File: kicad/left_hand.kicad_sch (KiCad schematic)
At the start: 31 parts, among them SW10 Gateron_ks_27, SW11 Gateron_ks_27, SW12 Gateron_ks_27, SW13 Gateron_ks_27, SW14 Gateron_ks_27, SW15 Gateron_ks_27, SW16 Gateron_ks_27, SW17 Gateron_ks_27, SW18 Gateron_ks_27, SW19 Gateron_ks_27, SW20 Gateron_ks_27, SW21 Gateron_ks_27, SW22 Gateron_ks_27, SW23 Gateron_ks_27, SW24 Gateron_ks_27, SW25 Gateron_ks_27, SW26 Gateron_ks_27, SW27 Gateron_ks_27, SW28 Gateron_ks_27, SW29 Gateron_ks_27, SW30 Gateron_ks_27, SW31 Gateron_ks_27, SW32 Gateron_ks_27, SW33 Gateron_ks_27, SW4 Gateron_ks_27, SW5 Gateron_ks_27, SW6 Gateron_ks_27, SW7 Gateron_ks_27, SW8 Gateron_ks_27, SW9 Gateron_ks_27, U2 74HC595

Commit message: Update PCB
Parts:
- added D1, D10, D11, D12, D13, D14, D15, D16, D17, D18, D19, D2, D20, D21, D22, D23, D24, D25, D26, D27, D28, D29, D3, D30, D4, D5, D6, D7, D8, D9: 1N4148W, Diode_SMD:D_SOD-123, symbol Diode:1N4148W-JLC
- SW10, SW11, SW12, SW13, SW14, SW15, SW16, SW17, SW18, SW19, SW20, SW21, SW22, SW23, SW24, SW25, SW26, SW27, SW28, SW29, SW30, SW31, SW32, SW33, SW4, SW5, SW6, SW7, SW8, SW9: now not fitted
- U2: LCSC (none) -> C72115
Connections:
- net ROW1: now also D1.1 (K), D2.1 (K), D3.1 (K), D4.1 (K), D5.1 (K), D6.1 (K), D7.1 (K); no longer SW10.3 (K), SW14.3 (K), SW18.3 (K), SW22.3 (K), SW26.3 (K), SW30.3 (K), SW6.3 (K)
- net ROW2: now also D10.1 (K), D11.1 (K), D12.1 (K), D13.1 (K), D14.1 (K), D8.1 (K), D9.1 (K); no longer SW11.3 (K), SW15.3 (K), SW19.3 (K), SW23.3 (K), SW27.3 (K), SW31.3 (K), SW7.3 (K)
- net ROW3: now also D15.1 (K), D16.1 (K), D17.1 (K), D18.1 (K), D19.1 (K), D20.1 (K), D21.1 (K), D22.1 (K); no longer SW12.3 (K), SW16.3 (K), SW20.3 (K), SW24.3 (K), SW28.3 (K), SW32.3 (K), SW4.3 (K), SW8.3 (K)
- net ROW4: now also D23.1 (K), D24.1 (K), D25.1 (K), D26.1 (K), D27.1 (K), D28.1 (K), D29.1 (K), D30.1 (K); no longer SW13.3 (K), SW17.3 (K), SW21.3 (K), SW25.3 (K), SW29.3 (K), SW33.3 (K), SW5.3 (K), SW9.3 (K)
- net at SW27.1: now also D13.2 (A); no longer SW27.4 (A)
- net at SW15.1: now also D10.2 (A); no longer SW15.4 (A)
- net at SW19.1: now also D11.2 (A); no longer SW19.4 (A)
- net at SW13.1: now also D25.2 (A); no longer SW13.4 (A)
- net at SW22.1: now also D5.2 (A); no longer SW22.4 (A)
- net at SW5.1: now also D23.2 (A); no longer SW5.4 (A)
- net at SW30.1: now also D7.2 (A); no longer SW30.4 (A)
- net at SW24.1: now also D20.2 (A); no longer SW24.4 (A)
- net at SW33.1: now also D30.2 (A); no longer SW33.4 (A)
- net at SW28.1: now also D21.2 (A); no longer SW28.4 (A)
- net at SW4.1: now also D15.2 (A); no longer SW4.4 (A)
- net at SW23.1: now also D12.2 (A); no longer SW23.4 (A)
- net at SW26.1: now also D6.2 (A); no longer SW26.4 (A)
- net at SW17.1: now also D26.2 (A); no longer SW17.4 (A)
- net at SW18.1: now also D4.2 (A); no longer SW18.4 (A)
- net at SW7.1: now also D8.2 (A); no longer SW7.4 (A)
- net at SW11.1: now also D9.2 (A); no longer SW11.4 (A)
- net at SW29.1: now also D29.2 (A); no longer SW29.4 (A)
- net at SW31.1: now also D14.2 (A); no longer SW31.4 (A)
- net at SW6.1: now also D1.2 (A); no longer SW6.4 (A)
- net at SW25.1: now also D28.2 (A); no longer SW25.4 (A)
- net at SW20.1: now also D19.2 (A); no longer SW20.4 (A)
- net at SW9.1: now also D24.2 (A); no longer SW9.4 (A)
- net at SW16.1: now also D18.2 (A); no longer SW16.4 (A)
- net at SW8.1: now also D16.2 (A); no longer SW8.4 (A)
- net at SW10.1: now also D2.2 (A); no longer SW10.4 (A)
- net at SW21.1: now also D27.2 (A); no longer SW21.4 (A)
- net at SW12.1: now also D17.2 (A); no longer SW12.4 (A)
- net at SW14.1: now also D3.2 (A); no longer SW14.4 (A)
- net at SW32.1: now also D22.2 (A); no longer SW32.4 (A)

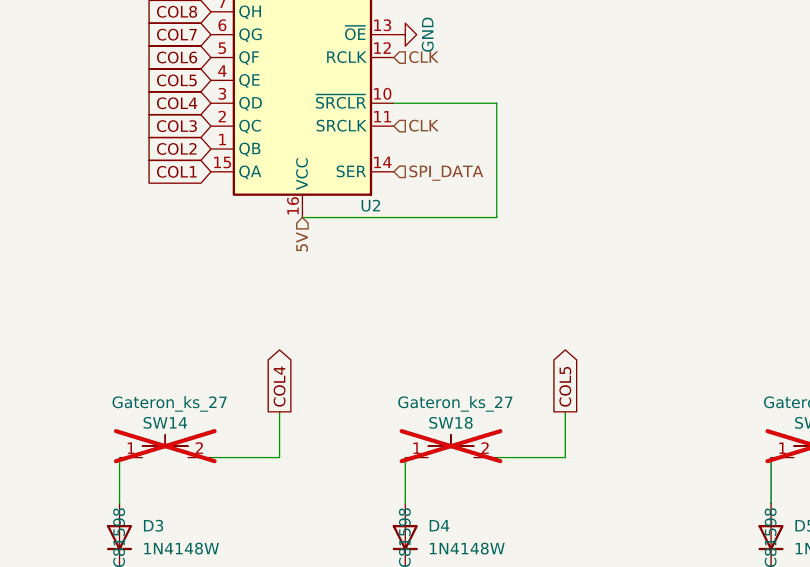
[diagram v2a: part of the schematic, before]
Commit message: SIPO is SMT
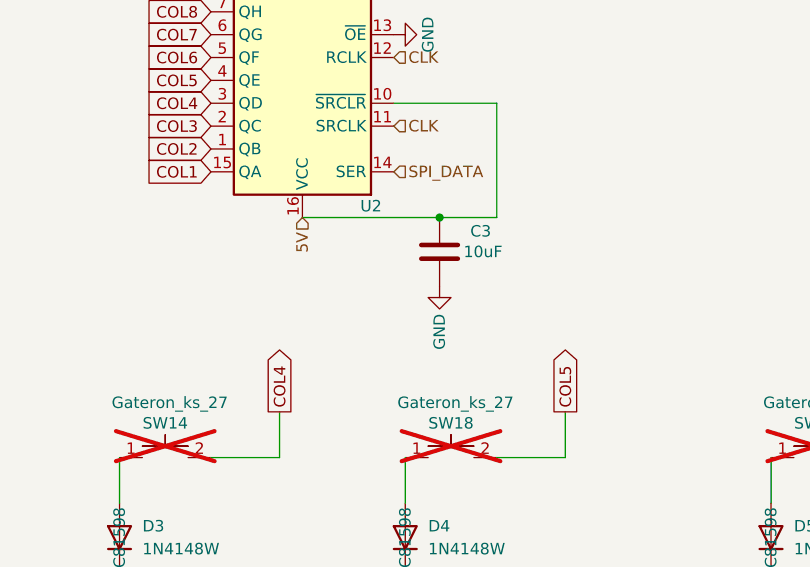
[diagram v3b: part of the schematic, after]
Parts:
- added C3: 10uF, Capacitor_SMD:C_0603_1608Metric, symbol Device:C
- U2: footprint Package_DIP:DIP-16_W7.62mm_Socket -> Package_SO:SO-16_3.9x9.9mm_P1.27mm; LCSC C72115 -> C5947
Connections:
- net 5V: now also C3.1
- net GND: now also C3.2
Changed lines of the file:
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@@
 	)
 	(junction
+		(at 208.28 90.17)
+		(diameter 0)
+		(color 0 0 0 0)
+	)
+	(junction
 		(at 107.95 227.33)
 		(diameter 0)
@@
 	(wire
 		(pts
-			(xy 214.63 90.17) (xy 193.04 90.17)
+			(xy 214.63 90.17) (xy 208.28 90.17)
 		)
 		(stroke
@@
 	(wire
 		(pts
+			(xy 208.28 90.17) (xy 193.04 90.17)
+		)
+		(stroke
+			(width 0)
+			(type default)
+		)
+	)
+	(wire
+		(pts
 			(xy 140.97 227.33) (xy 172.72 227.33)
 		)
@@
 	(symbol
 		(lib_id "power:GND")
+		(at 208.28 97.79 0)
+		(unit 1)
+		(exclude_from_sim no)
+		(in_bom yes)
+		(on_board yes)
+		(dnp no)
+		(property "Reference" "#PWR05"
+			(at 208.28 104.14 0)
+			(effects
+				(font
+					(size 1.27 1.27)
+				)
+				(hide yes)
+			)
+		)
+		(property "Value" "GND"
+			(at 208.28 102.87 90)
+			(effects
+				(font
+					(size 1.27 1.27)
+				)
+			)
+		)
+		(property "Footprint" ""
+			(at 208.28 97.79 0)
+			(effects
+				(font
+					(size 1.27 1.27)
+				)
+				(hide yes)
+			)
+		)
+		(property "Datasheet" ""
+			(at 208.28 97.79 0)
+			(effects
+				(font
+					(size 1.27 1.27)
+				)
+				(hide yes)
+			)
+		)
+		(property "Description" "Power symbol creates a global label with name \"GND\" , ground"
+			(at 208.28 97.79 0)
+			(effects
+				(font
+					(size 1.27 1.27)
+				)
+				(hide yes)
+			)
+		)
+		(pin "1"
+		)
+		(instances
+			(project "keyboard"
+				(path "/b0ce3c94-e169-4400-82ce-8ef44a8a59a3/f6761ea6-a0c4-4238-8bcb-bb4bd82c6051"
+					(reference "#PWR05")
+					(unit 1)
+				)
+			)
+		)
+	)
+	(symbol
+		(lib_id "power:GND")
 		(at 193.04 57.15 180)
 		(unit 1)
@@
 			)
 		)
-		(property "Footprint" "Package_DIP:DIP-16_W7.62mm_Socket"
+		(property "Footprint" "Package_SO:SO-16_3.9x9.9mm_P1.27mm"
 			(at 193.04 74.93 0)
 			(effects
@@
 			)
 		)
-		(property "LCSC" "C72115"
+		(property "LCSC" "C5947"
 			(at 193.04 74.93 0)
 			(effects
@@
 					(unit 1)
 				)
+			)
+		)
+	)
+	(symbol
+		(lib_id "Device:C")
+		(at 208.28 93.98 0)
+		(unit 1)
+		(exclude_from_sim no)
+		(in_bom yes)
+		(on_board yes)
+		(dnp no)
+		(property "Reference" "C3"
+			(at 212.852 91.694 0)
+			(effects
+				(font
+					(size 1.27 1.27)
+				)
+			)
+		)
+		(property "Value" "10uF"
+			(at 213.106 93.98 0)
+			(effects
+				(font
+					(size 1.27 1.27)
+				)
+			)
+		)
+		(property "Footprint" "Capacitor_SMD:C_0603_1608Metric"
+			(at 209.2452 97.79 0)
+			(effects
+				(font
+					(size 1.27 1.27)
+				)
+				(hide yes)
+			)
+		)
+		(property "Datasheet" "~"
+			(at 208.28 93.98 0)
+			(effects
+				(font
+					(size 1.27 1.27)
+				)
+				(hide yes)
+			)
+		)
+		(property "Description" ""
+			(at 208.28 93.98 0)
+			(effects
+				(font
+					(size 1.27 1.27)
+				)
+				(hide yes)
+			)
+		)
+		(property "LCSC" "C19702"
+			(at 208.28 93.98 90)
+			(effects
+				(font
+					(size 1.27 1.27)
+				)
+				(hide yes)
+			)
+		)
+		(pin "1"
+		)
+		(pin "2"
+		)
+		(instances
+			(project "keyboard"
+				(path "/b0ce3c94-e169-4400-82ce-8ef44a8a59a3/f6761ea6-a0c4-4238-8bcb-bb4bd82c6051"
+					(reference "C3")
+					(unit 1)
+				)
